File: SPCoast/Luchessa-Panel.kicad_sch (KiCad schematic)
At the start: 21 parts, among them SW8784 783, SW8796 795, SW8800 799, U8004 0x24, U8005 0x25, U8006 0x26

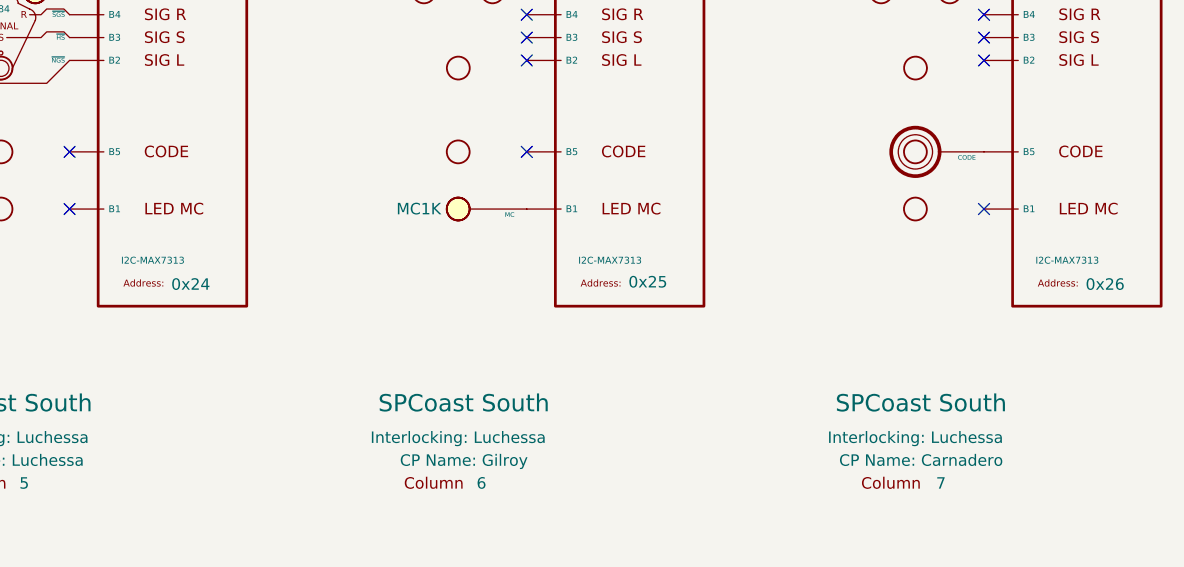
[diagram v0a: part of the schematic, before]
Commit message: chore(kicad): SPCoast symbols refreshed, field attribute visibility, no-connects on unused pins (owner's edit, baseline)
Owner, 2026-10-08: updated symbols from the libraries (the field pin direction flip, InterlockingPlant
61269e0), adjusted attribute visibility, added 22 no-connect markers on unused pins.

Verified (committed as saved, no edits):
- 485 components, 648 nets; every net identical to the previous commit.
- ERC 53 -> 20 messages (13 errors, 7 warnings). Remaining: unconnected HOUSE H / aux MC pins
  (Gilroy Caltrain, Luchessa, Watsonville); Corporal SW11901 still Railroad:Switch_HandThrow (not in
  the library) with open N/R legs; Sargent switch 1 open N/R legs; Christopher Panel U10029 A6 open
  while lamp LMP10093 carries a no-connect; 5 inherited wire stubs.
- Every instance path starts at the root uuid.

Co-Authored-By: Claude Opus 5.5 <noreply@anthropic.com>
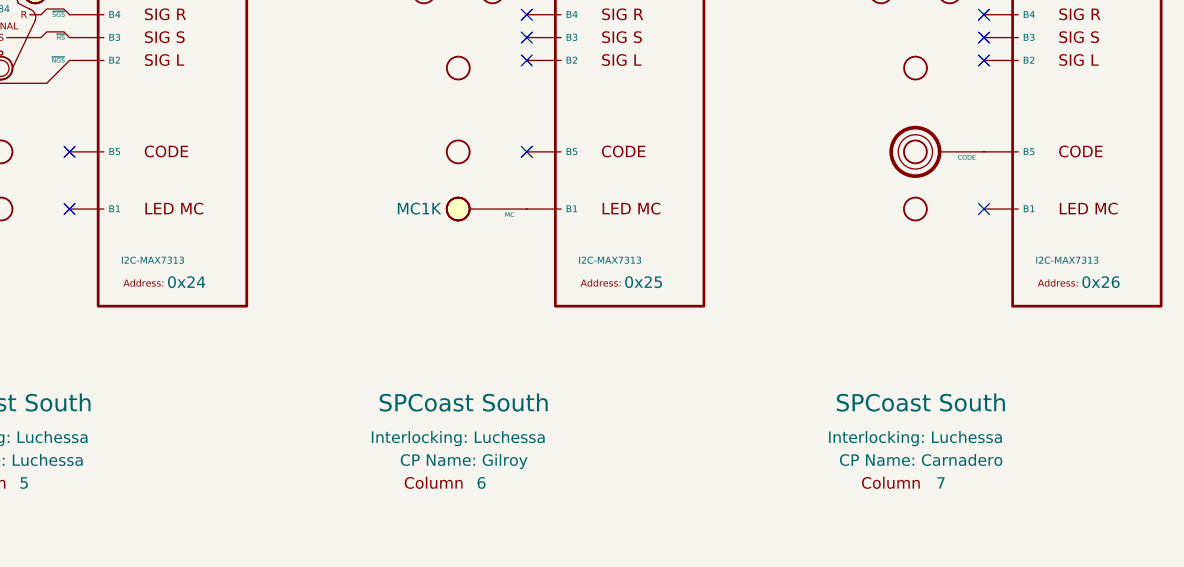
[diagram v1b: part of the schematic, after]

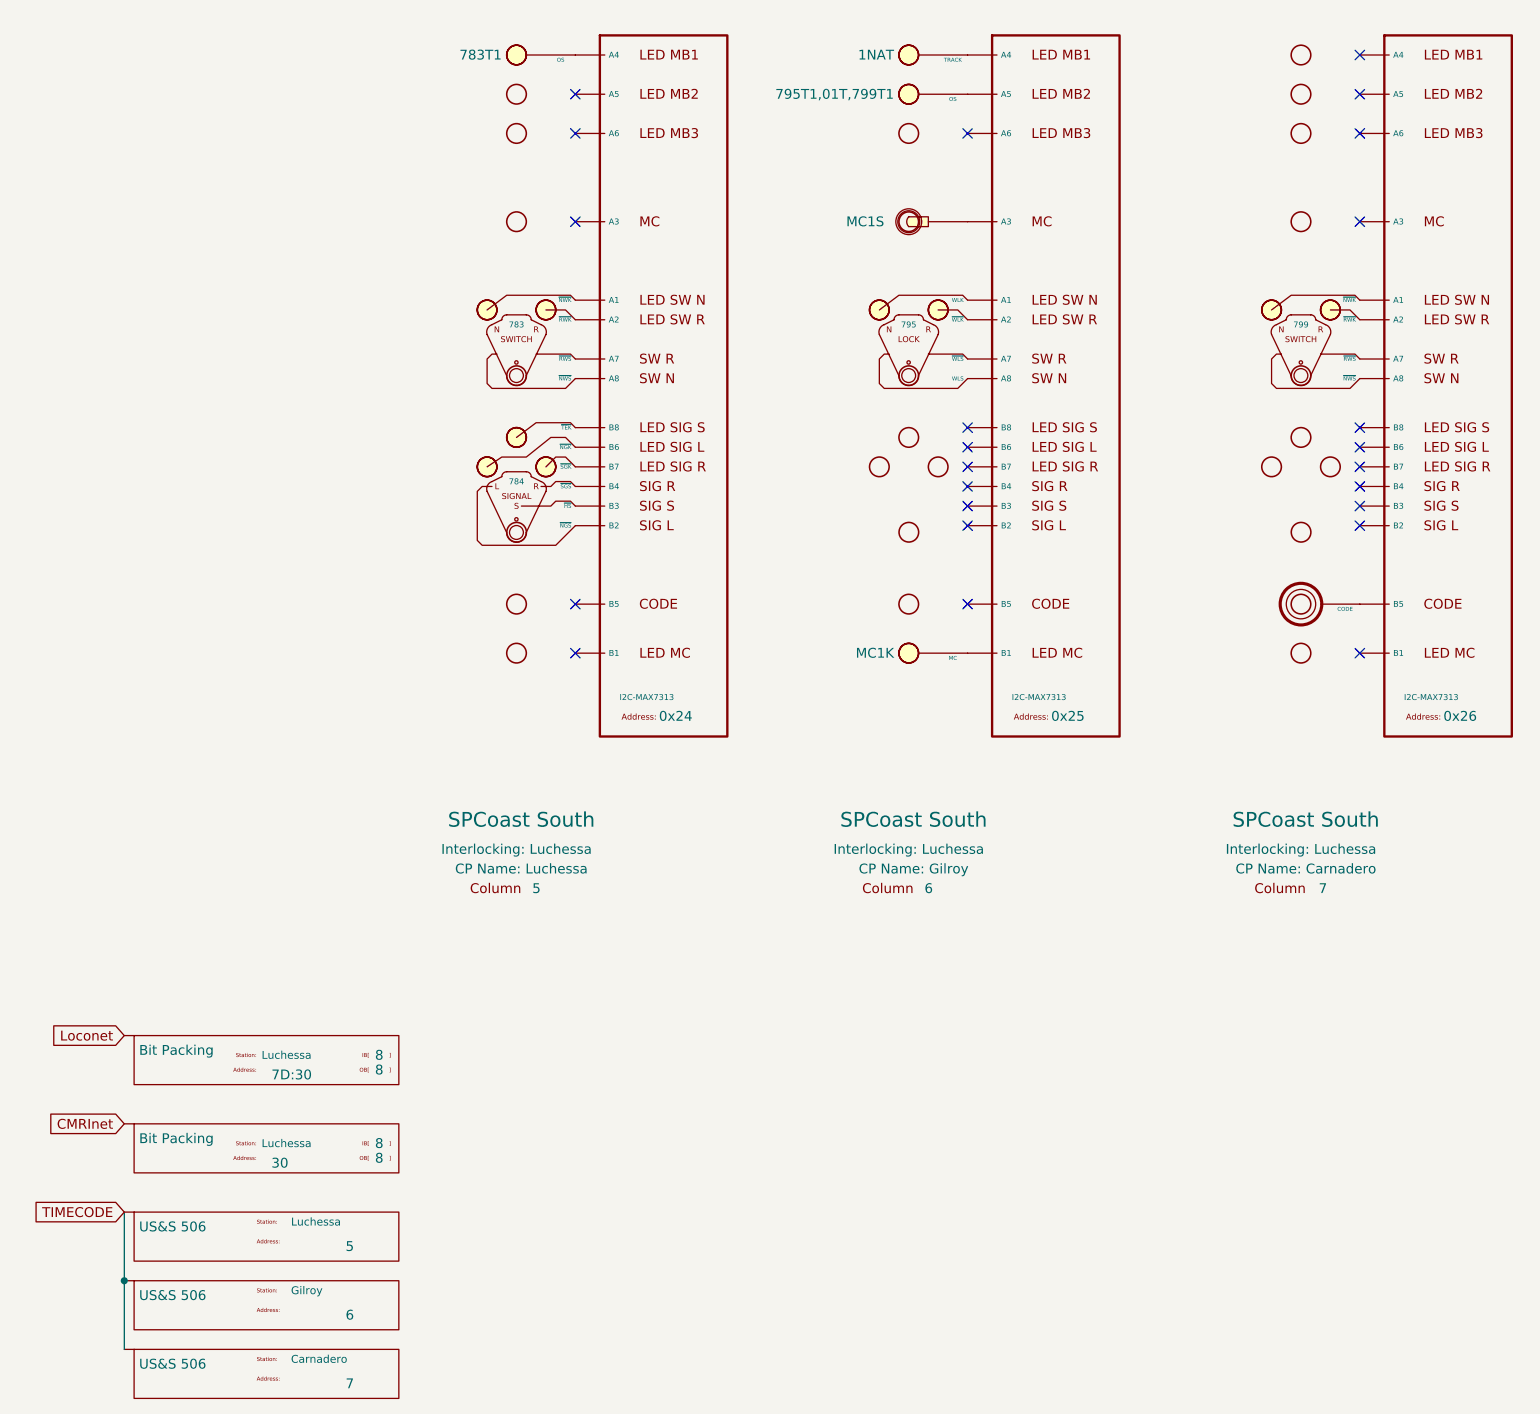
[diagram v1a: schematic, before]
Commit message: feat(spcoast): every sheet on the four Railroad libraries (checkpoint step 6, mechanical half)
By SPCoast/edits/2026-10-12-migrate-libraries.py, run once with KiCad closed: 483 instances
remapped across 16 sheets, embedded definitions replaced by the library blocks, instance fields
synced (Kind, ControlToken, Vital, NormalIs, Chain, Index dropped; Indications renamed
IndicationCeiling; Hold_ms renamed hold_ms; a pixel's Index became its Address; Rulebook kept
on the four Luchessa markers because the compiler still reads it), and 22 units added at the
same position for the plates and devices that are multi-unit now. Owner's choices: every plant
head CPL; Sargent's semaphore UQ; the 0x27 PCA9685 as PWM; the office MAX7313s as the
SPCoastcTc variant. Left by hand: the two AUXILIARY_TRAFFIC markers on Watsonville (retired).

Verified (production/migration-gate.txt, netlist_diff.py against pre-migration.net): office
and local plates and all chips keep their connectivity; 14 nets lost, all on Sargent, where
the six field devices (DevSW13001, 13004 to 13007, 13012) have new pin positions and must be
re-wired by hand. ERC: lib_symbol_issues 492 before (unregistered libraries) to 2 after (the
retired markers); the 29 unconnected pins are those devices and their chip pins.

Co-Authored-By: Claude Fable 5.1 <noreply@anthropic.com>
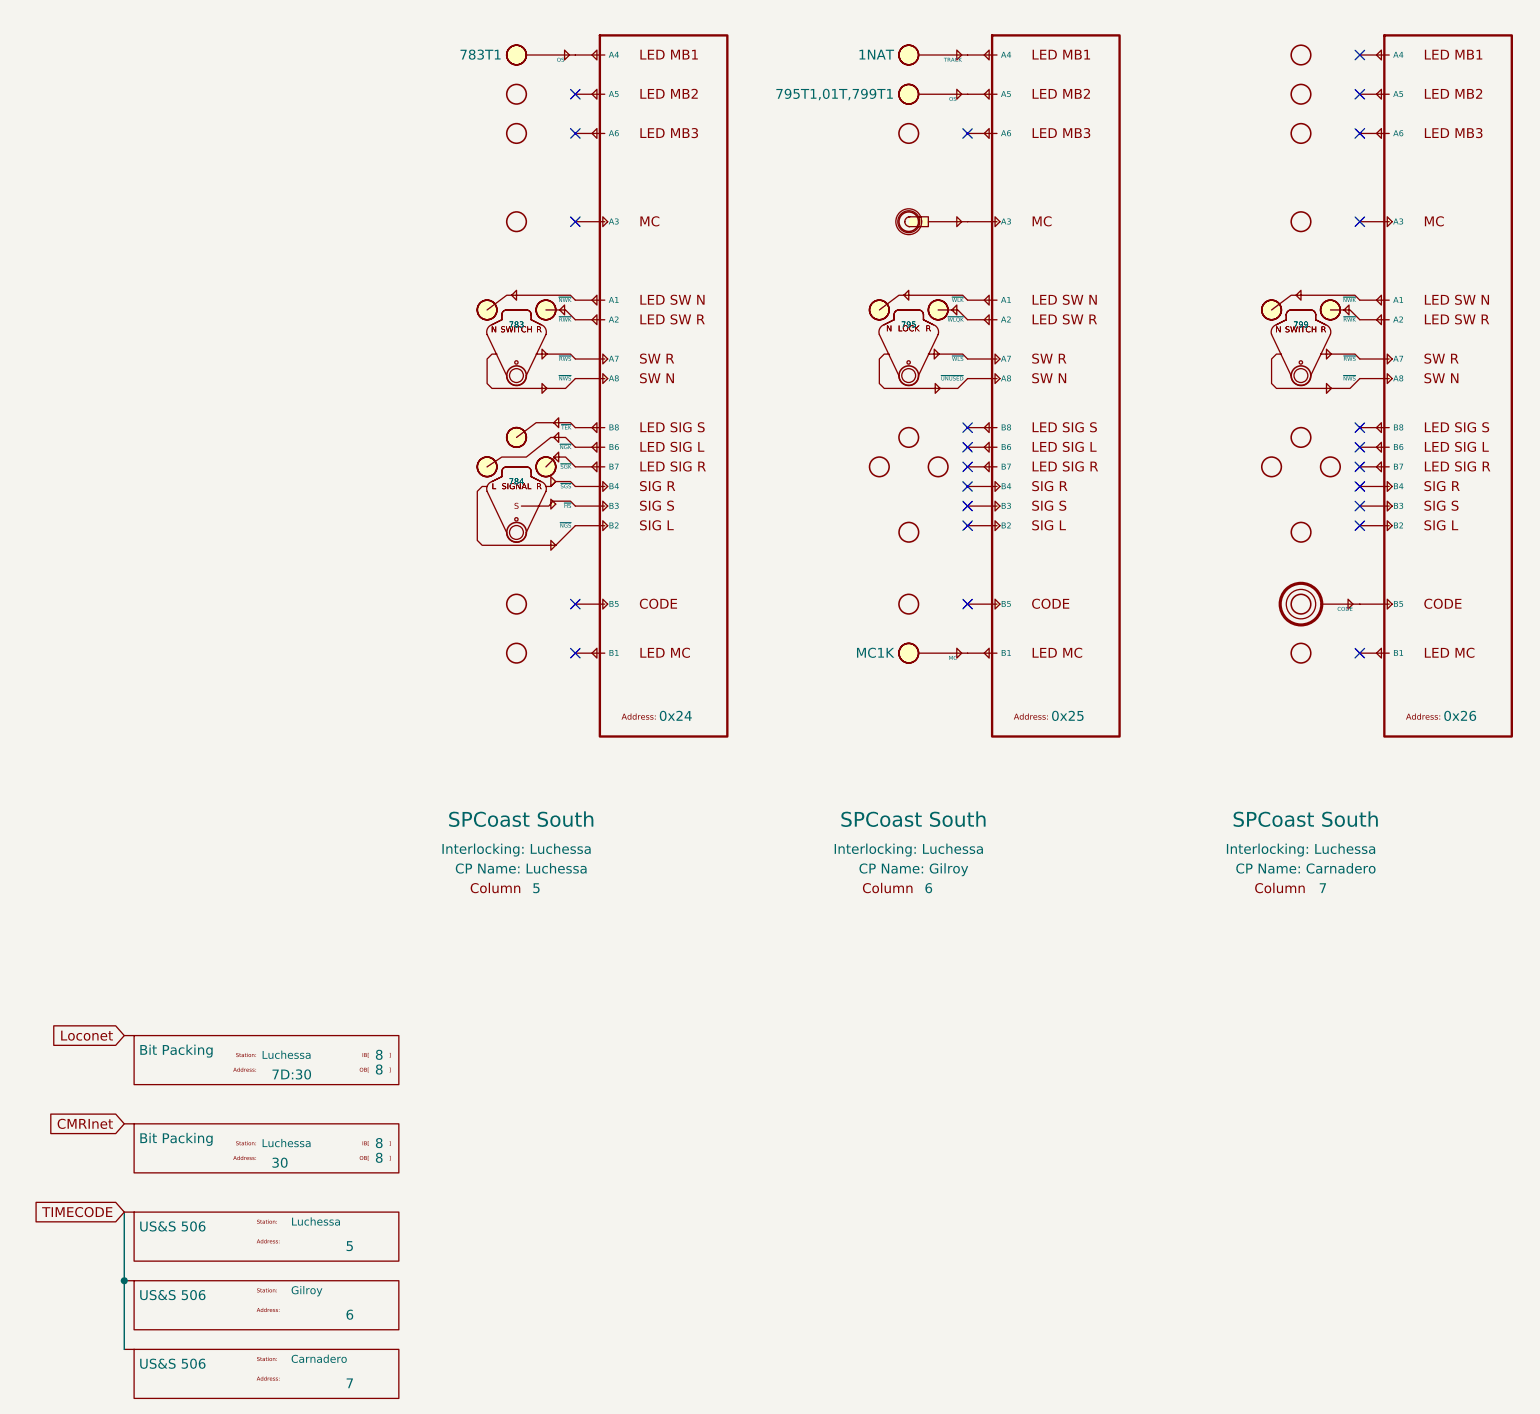
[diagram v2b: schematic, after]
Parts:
- added unit 2 of SIG8785
- added unit 2 of SW8784
- added unit 2 of SW8796
- added unit 2 of SW8800
- AUX8002: symbol RailroadPanel:PanelMCall -> Railroad-Office:PanelMCall; Appliance (none) -> lever; ControlToken MC1S -> (none); Kind MAINTAINER_CALL -> (none); Pin.S (none) -> binary; Style (none) -> maintainer_call; Vital NO -> (none)
- CODE8002: symbol RailroadPanel:PanelCode -> Railroad-Office:PanelCode; Appliance (none) -> lever; Kind CODE -> (none); Pin.CODE (none) -> binary; Style (none) -> code
- COL8004, COL8005, COL8006: symbol RailroadPanel:PanelColumn -> Railroad-Office:PanelColumn
- Encoding8002, Encoding8003, Encoding8004: symbol RailroadPanel:Codeline-Encoding-US&S-506 -> Railroad-Office:Codeline-Encoding-US&S-506
- Encoding8005, Encoding8006: symbol RailroadPanel:Codeline-Encoding-Bits -> Railroad-Office:Codeline-Encoding-Bits
- LAMP8005, LAMP8007: symbol RailroadPanel:PanelLamp-RED -> Railroad-Office:PanelLamp-RED; Appliance (none) -> lamp; Kind LAMP -> (none); Pin.LAMP (none) -> binary; Style (none) -> indication
- LAMP8006, LAMP8008: symbol RailroadPanel:PanelLamp-YELLOW -> Railroad-Office:PanelLamp-YELLOW; Appliance (none) -> lamp; Kind LAMP -> (none); Pin.LAMP (none) -> binary; Style (none) -> indication
- SIG8785: symbol RailroadPanel:PanelSignal -> Railroad-Office:PanelSignal; Appliance (none) -> lever; Kind SIGNAL_LEVER -> (none); Pin.HS (none) -> binary; Pin.NGK (none) -> binary; Pin.NGS (none) -> binary; Pin.SGK (none) -> binary; Pin.SGS (none) -> binary; Pin.TEK (none) -> binary; Style (none) -> signal
- SW8784, SW8800: symbol RailroadPanel:PanelSwitch -> Railroad-Office:PanelSwitch; Appliance (none) -> lever; Kind SWITCH_LEVER -> (none); Pin.NWK (none) -> binary; Pin.NWS (none) -> binary; Pin.RWK (none) -> binary; Pin.RWS (none) -> binary; Style (none) -> switch
- SW8796: symbol RailroadPanel:PanelLock -> Railroad-Office:PanelLock; Appliance (none) -> lever; Invert (none) -> WLK; Kind LOCK_LEVER_2LAMP_2CONTACT -> (none); Pin.UNUSED (none) -> binary; Pin.WLK (none) -> binary; Pin.WLQK (none) -> binary; Pin.WLS (none) -> binary; Style (none) -> lock
- U8004, U8005, U8006: symbol RailroadPanel:Driver-I2C-MAX7313 -> Railroad-HardwareIO:Driver-I2C-MAX7313-SPCoastcTc; IC (none) -> MAX7313; Kind I2C-MAX7313 -> (none); Pin.A1 (none) -> binary; Pin.A2 (none) -> binary; Pin.A3 (none) -> binary; Pin.A4 (none) -> binary; Pin.A5 (none) -> binary; Pin.A6 (none) -> binary; Pin.A7 (none) -> binary; Pin.A8 (none) -> binary; Pin.B1 (none) -> binary; Pin.B2 (none) -> binary; Pin.B3 (none) -> binary; Pin.B4 (none) -> binary; Pin.B5 (none) -> binary; Pin.B6 (none) -> binary; Pin.B7 (none) -> binary; Pin.B8 (none) -> binary
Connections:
- net at U8005.2 (A2): now also SW8796.4 (~{WLQK}); no longer SW8796.4 (~{WLK})
- net at U8005.1 (A1): now also SW8796.5 (~{WLK}); no longer SW8796.5 (WLK)
- net at U8004.2 (A2): now also SW8784.4 (~{RWK}); no longer SW8784.4 (~{RWK})
- net at U8004.1 (A1): now also SW8784.5 (~{NWK}); no longer SW8784.5 (~{NWK})
- net at U8006.2 (A2): now also SW8800.4 (~{RWK}); no longer SW8800.4 (~{RWK})
- net at U8006.1 (A1): now also SW8800.5 (~{NWK}); no longer SW8800.5 (~{NWK})
- net at U8004.14 (B6): now also SIG8785.6 (~{NGK}); no longer SIG8785.6 (~{NGK})
- net at U8004.15 (B7): now also SIG8785.5 (~{SGK}); no longer SIG8785.5 (~{SGK})
- net at U8004.16 (B8): now also SIG8785.7 (~{TEK}); no longer SIG8785.7 (~{TEK})

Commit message: chore: owner's Sargent cleanup and library edits of 2026-10-12 and 13 (baseline)
Co-Authored-By: Claude Fable 5.1 <noreply@anthropic.com>
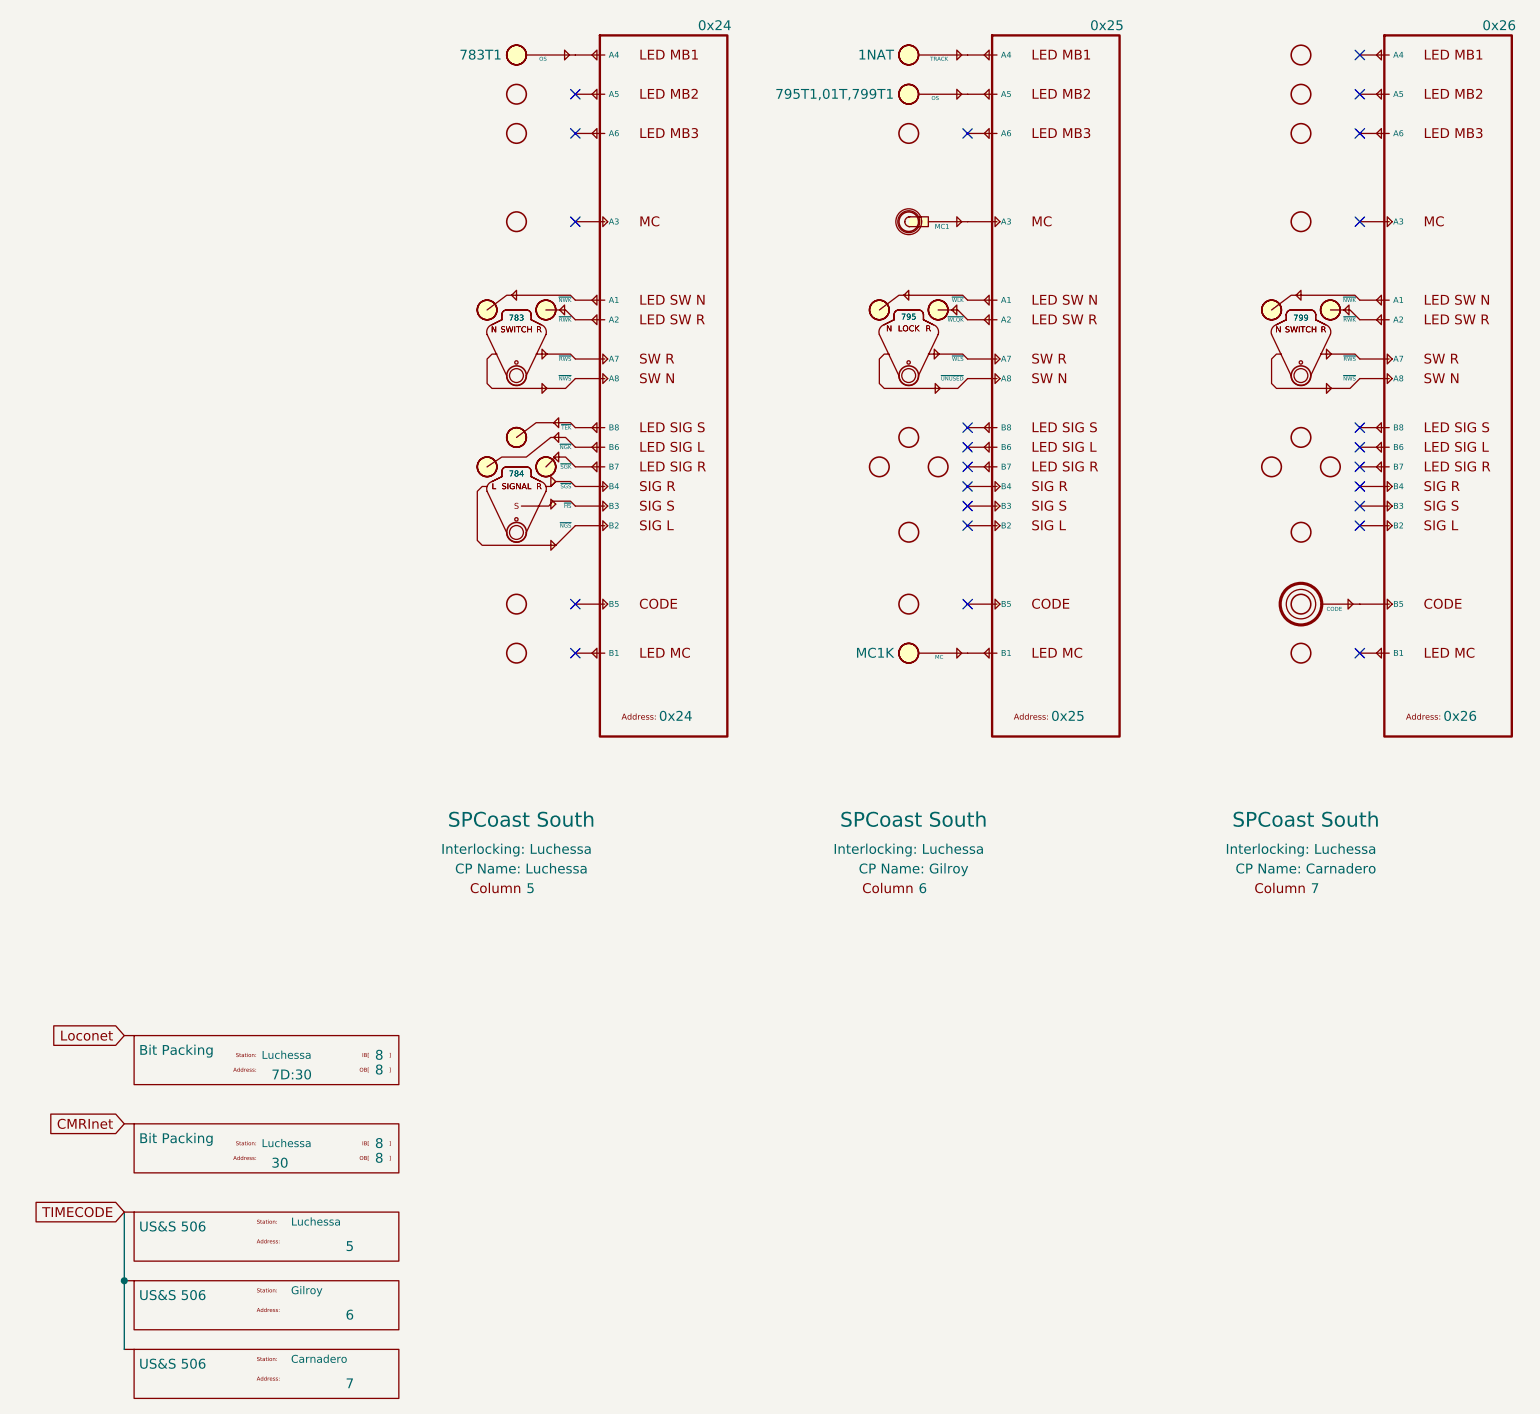
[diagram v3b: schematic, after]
